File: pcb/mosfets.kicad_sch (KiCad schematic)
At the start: 21 parts, among them IC2 IRFR9014PBF, J15 Arm, J4 Screw_Terminal_01x12, Q1 DMN3404L, Q2 DMN3404L, Q3 DMN3404L, Q4 DMN3404L, Q5 DMN3404L, Q7 MMBT2222A, Q8 DMN3404L

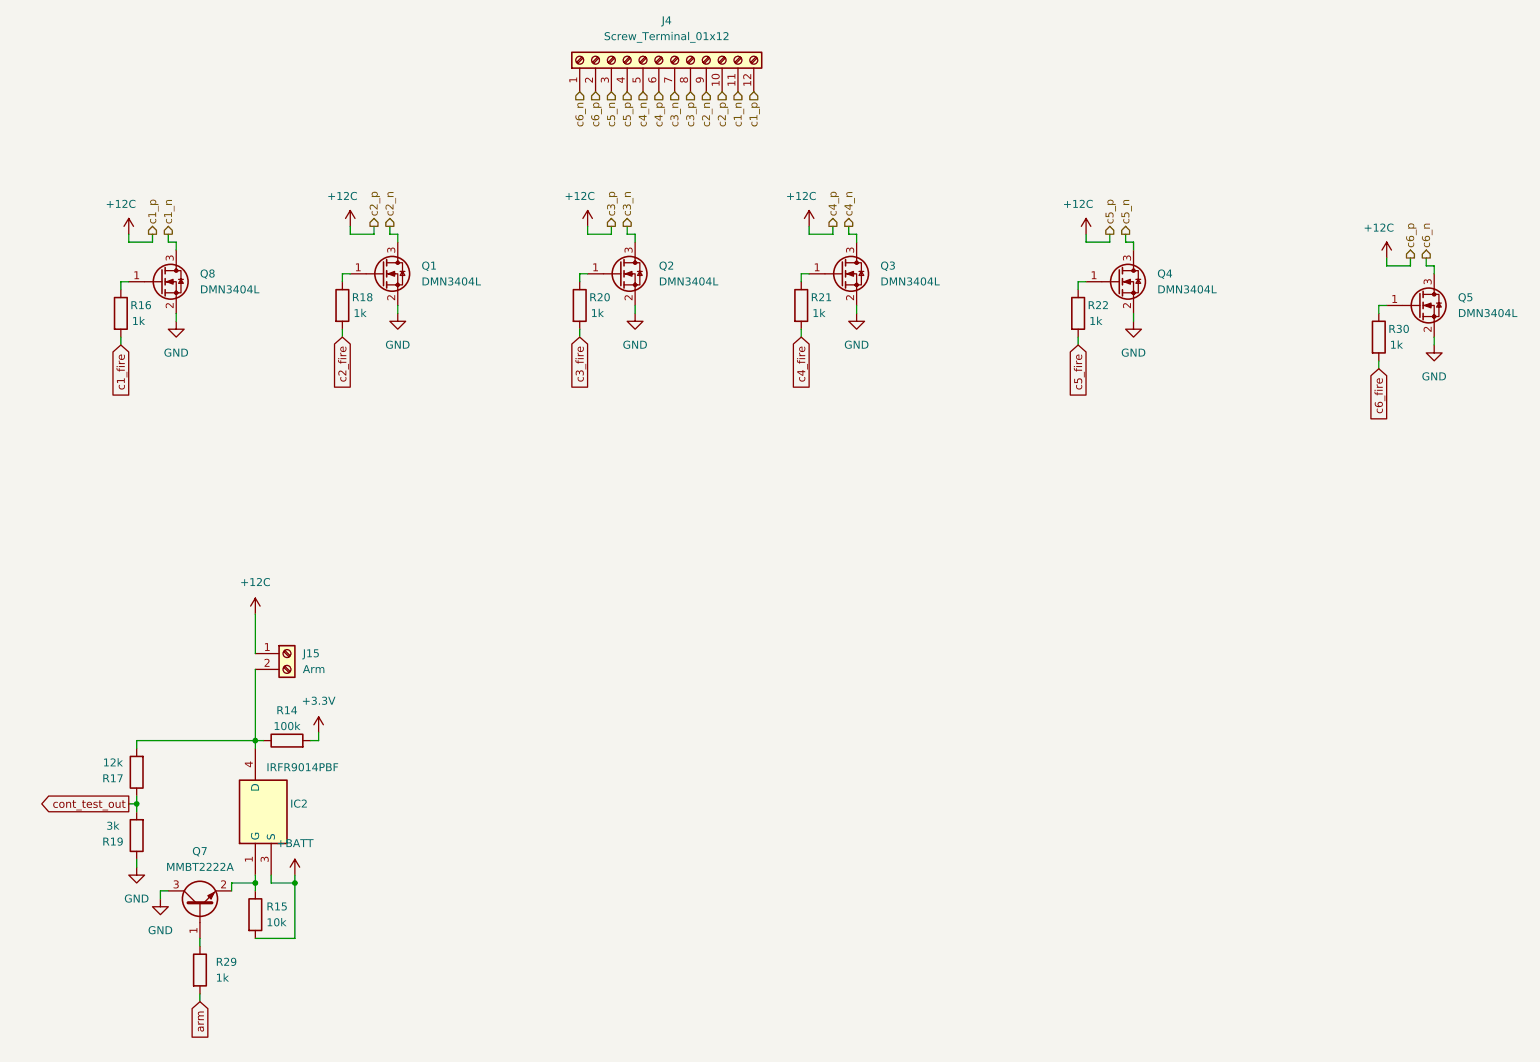
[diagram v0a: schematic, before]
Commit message: added models for some things, fixed micro sd impl and a bunch of other stuff - pcb currently probably ready for production
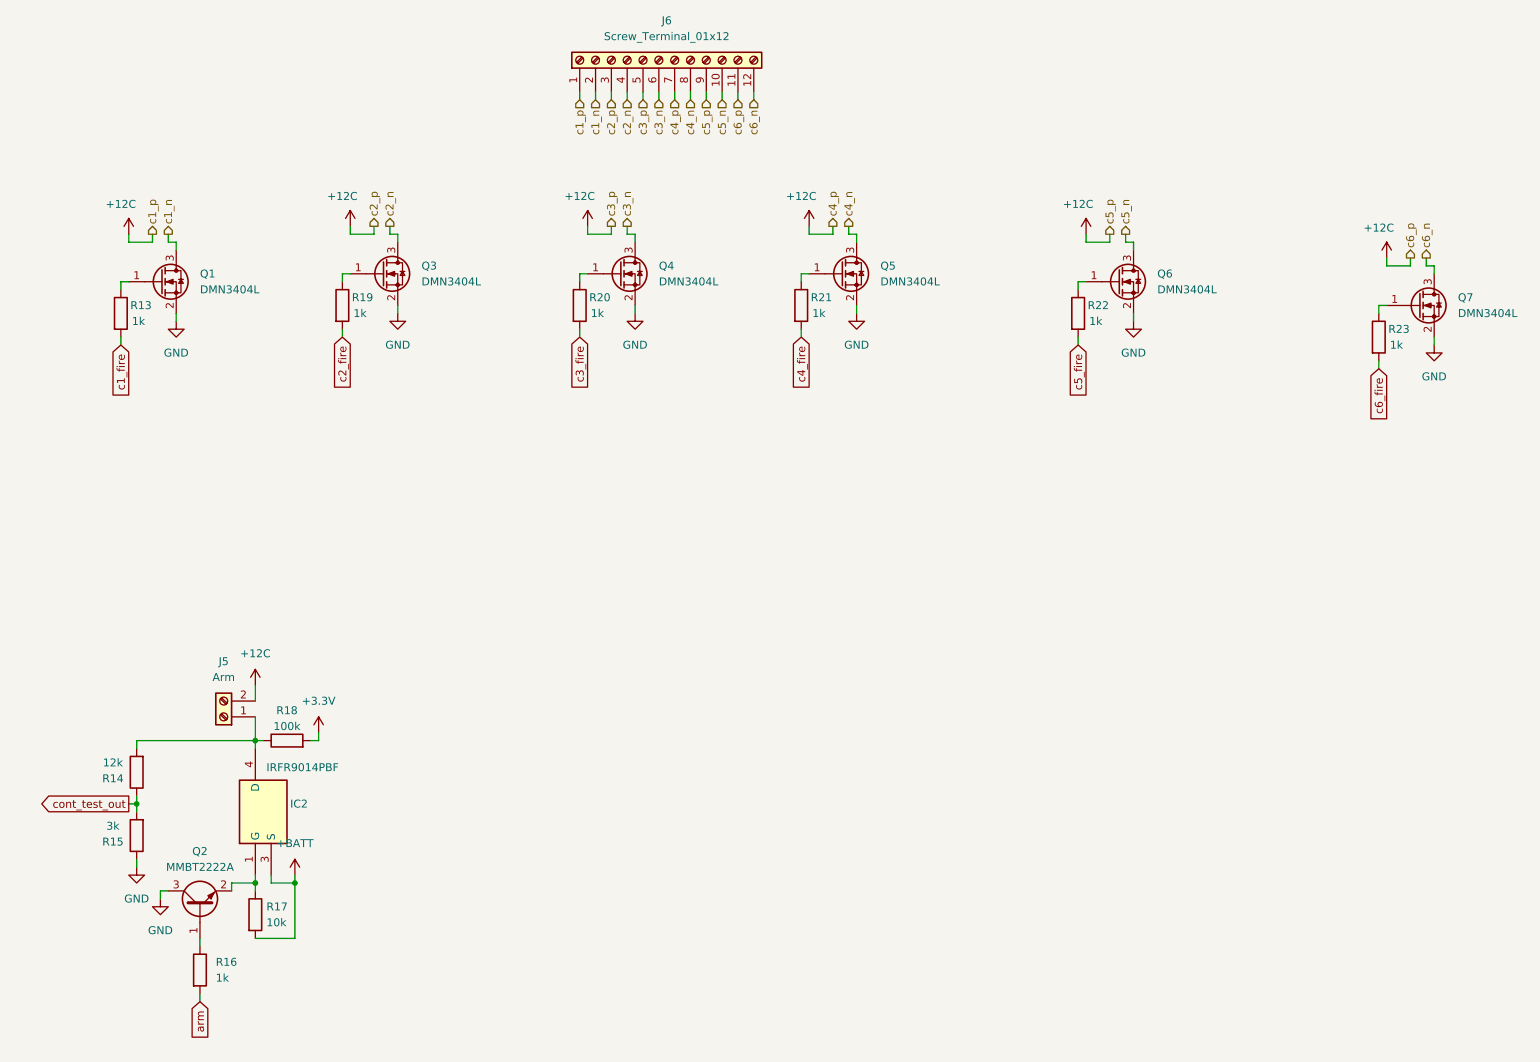
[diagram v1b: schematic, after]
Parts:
- renumbered J15 to J5, J4 to J6, Q8 to Q1, Q7 to Q2, Q1 to Q3, Q2 to Q4, Q3 to Q5, Q4 to Q6, Q5 to Q7, R16 to R13, R17 to R14, R19 to R15, R29 to R16, R15 to R17, R14 to R18, R18 to R19, R30 to R23
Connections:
- net +12C: now also J5.2 (Pin_2), J6.1 (Pin_1), J6.11 (Pin_11), J6.3 (Pin_3), J6.5 (Pin_5), J6.7 (Pin_7), J6.9 (Pin_9); no longer J5.1 (Pin_1), J6.10 (Pin_10), J6.12 (Pin_12), J6.2 (Pin_2), J6.4 (Pin_4), J6.6 (Pin_6), J6.8 (Pin_8)
- net c1_n: now also J6.2 (Pin_2); no longer J6.11 (Pin_11)
- net c2_n: now also J6.4 (Pin_4); no longer J6.9 (Pin_9)
- net c3_n: now also J6.6 (Pin_6); no longer J6.7 (Pin_7)
- net c4_n: now also J6.8 (Pin_8); no longer J6.5 (Pin_5)
- net c5_n: now also J6.10 (Pin_10); no longer J6.3 (Pin_3)
- net c6_n: now also J6.12 (Pin_12); no longer J6.1 (Pin_1)
- net at IC2.4 (D), R14.2, R18.1: now also J5.1 (Pin_1); no longer J5.2 (Pin_2)
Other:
- moved on the sheet: J5

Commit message: updated pcb from schematic changes, also added some length tuning because why not
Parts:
- renumbered J5 to ARM1, J6 to PYRO1
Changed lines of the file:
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@@
 		(dnp no)
 		(fields_autoplaced yes)
-		(property "Reference" "J6"
+		(property "Reference" "PYRO1"
 			(at 125.73 22.86 90)
 			(effects
@@
 			(project ""
 				(path "/d0cafa98-cc2a-4ab3-8dbc-f937bedf434b/95cda17b-9612-4f29-a3fa-5878468b6ce9"
-					(reference "J6")
+					(reference "PYRO1")
 					(unit 1)
 				)
@@
 		(dnp no)
 		(fields_autoplaced yes)
-		(property "Reference" "J5"
+		(property "Reference" "ARM1"
 			(at 54.61 125.73 0)
 			(effects
@@
 			(project ""
 				(path "/d0cafa98-cc2a-4ab3-8dbc-f937bedf434b/95cda17b-9612-4f29-a3fa-5878468b6ce9"
-					(reference "J5")
-					(unit 1)
-				)
+					(reference "ARM1")
+					(unit 1)
+				)

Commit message: mainly worked on bom (still just on google sheets), but while doing so fixed some issues and redid some component selection
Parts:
- removed PYRO1: Screw_Terminal_01x12, TerminalBlock:TerminalBlock_Xinya_XY308-2.54-12P_1x12_P2.54mm_Horizontal, symbol Connector:Screw_Terminal_01x12
- added PYRO1, PYRO2: Screw_Terminal_01x06, footprints:TBC05061GG, symbol Connector:Screw_Terminal_01x06
- ARM1: footprint TerminalBlock:TerminalBlock_Xinya_XY308-2.54-2P_1x02_P2.54mm_Horizontal -> footprints:TBC05021GG
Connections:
- net +12C: now also PYRO1.1 (Pin_1), PYRO1.3 (Pin_3), PYRO1.5 (Pin_5), PYRO2.1 (Pin_1), PYRO2.3 (Pin_3), PYRO2.5 (Pin_5)
- net c1_n: now also PYRO1.2 (Pin_2)
- net c2_n: now also PYRO1.4 (Pin_4)
- net c3_n: now also PYRO1.6 (Pin_6)
- net c4_n: now also PYRO2.2 (Pin_2)
- net c5_n: now also PYRO2.4 (Pin_4)
- net c6_n: now also PYRO2.6 (Pin_6)
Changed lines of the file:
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@@
-	)
-	(symbol
-		(lib_id "Connector:Screw_Terminal_01x12")
-		(at 124.46 29.21 90)
-		(unit 1)
-		(exclude_from_sim no)
-		(in_bom yes)
-		(on_board yes)
-		(dnp no)
-		(fields_autoplaced yes)
-		(property "Reference" "PYRO1"
-			(at 125.73 22.86 90)
-			(effects
-				(font
-					(size 1.27 1.27)
-				)
-			)
-		)
-		(property "Value" "Screw_Terminal_01x12"
-			(at 125.73 25.4 90)
-			(effects
-				(font
-					(size 1.27 1.27)
-				)
-			)
-		)
-		(property "Footprint" "TerminalBlock:TerminalBlock_Xinya_XY308-2.54-12P_1x12_P2.54mm_Horizontal"
-			(at 124.46 29.21 0)
-			(effects
-				(font
-					(size 1.27 1.27)
-				)
-				(hide yes)
-			)
-		)
-		(property "Datasheet" "~"
-			(at 124.46 29.21 0)
-			(effects
-				(font
-					(size 1.27 1.27)
-				)
-				(hide yes)
-			)
-		)
-		(property "Description" "Generic screw terminal, single row, 01x12, script generated (kicad-library-utils/schlib/autogen/connector/)"
-			(at 124.46 29.21 0)
-			(effects
-				(font
-					(size 1.27 1.27)
-				)
-				(hide yes)
-			)
-		)
-		(pin "6"
-		)
-		(pin "10"
-		)
-		(pin "1"
-		)
-		(pin "7"
-		)
-		(pin "5"
-		)
-		(pin "4"
-		)
-		(pin "3"
-		)
-		(pin "12"
-		)
-		(pin "11"
-		)
-		(pin "2"
-		)
-		(pin "9"
-		)
-		(pin "8"
-		)
-		(instances
-			(project ""
-				(path "/d0cafa98-cc2a-4ab3-8dbc-f937bedf434b/95cda17b-9612-4f29-a3fa-5878468b6ce9"
-					(reference "PYRO1")
-					(unit 1)
-				)
-			)
-		)
 	)
 	(symbol
@@
 	)
 	(symbol
+		(lib_id "Connector:Screw_Terminal_01x06")
+		(at 116.84 29.21 90)
+		(unit 1)
+		(exclude_from_sim no)
+		(in_bom yes)
+		(on_board yes)
+		(dnp no)
+		(fields_autoplaced yes)
+		(property "Reference" "PYRO1"
+			(at 118.11 22.86 90)
+			(effects
+				(font
+					(size 1.27 1.27)
+				)
+			)
+		)
+		(property "Value" "Screw_Terminal_01x06"
+			(at 118.11 25.4 90)
+			(effects
+				(font
+					(size 1.27 1.27)
+				)
+			)
+		)
+		(property "Footprint" "footprints:TBC05061GG"
+			(at 116.84 29.21 0)
+			(effects
+				(font
+					(size 1.27 1.27)
+				)
+				(hide yes)
+			)
+		)
+		(property "Datasheet" "~"
+			(at 116.84 29.21 0)
+			(effects
+				(font
+					(size 1.27 1.27)
+				)
+				(hide yes)
+			)
+		)
+		(property "Description" "Generic screw terminal, single row, 01x06, script generated (kicad-library-utils/schlib/autogen/connector/)"
+			(at 116.84 29.21 0)
+			(effects
+				(font
+					(size 1.27 1.27)
+				)
+				(hide yes)
+			)
+		)
+		(pin "2"
+		)
+		(pin "1"
+		)
+		(pin "3"
+		)
+		(pin "6"
+		)
+		(pin "5"
+		)
+		(pin "4"
+		)
+		(instances
+			(project ""
+				(path "/d0cafa98-cc2a-4ab3-8dbc-f937bedf434b/95cda17b-9612-4f29-a3fa-5878468b6ce9"
+					(reference "PYRO1")
+					(unit 1)
+				)
+			)
+		)
+	)
+	(symbol
 		(lib_id "Device:R")
 		(at 38.1 69.85 0)
@@
 			)
 		)
-		(property "Footprint" "TerminalBlock:TerminalBlock_Xinya_XY308-2.54-2P_1x02_P2.54mm_Horizontal"
+		(property "Footprint" "footprints:TBC05021GG"
 			(at 54.61 134.62 0)
 			(effects
@@
 					(unit 1)
 				)
+			)
+		)
+	)
+	(symbol
+		(lib_id "Connector:Screw_Terminal_01x06")
+		(at 132.08 29.21 90)
+		(unit 1)
+		(exclude_from_sim no)
+		(in_bom yes)
+		(on_board yes)
+		(dnp no)
+		(fields_autoplaced yes)
+		(property "Reference" "PYRO2"
+			(at 133.35 22.86 90)
+			(effects
+				(font
+					(size 1.27 1.27)
+				)
+			)
+		)
+		(property "Value" "Screw_Terminal_01x06"
+			(at 133.35 25.4 90)
+			(effects
+				(font
+					(size 1.27 1.27)
+				)
+			)
+		)
+		(property "Footprint" "footprints:TBC05061GG"
+			(at 132.08 29.21 0)
+			(effects
+				(font
+					(size 1.27 1.27)
+				)
+				(hide yes)
+			)
+		)
+		(property "Datasheet" "~"
+			(at 132.08 29.21 0)
+			(effects
+				(font
+					(size 1.27 1.27)
+				)
+				(hide yes)
+			)
+		)
+		(property "Description" "Generic screw terminal, single row, 01x06, script generated (kicad-library-utils/schlib/autogen/connector/)"
+			(at 132.08 29.21 0)
+			(effects
+				(font
+					(size 1.27 1.27)
+				)
+				(hide yes)
+			)
+		)
+		(pin "2"
+		)
+		(pin "1"
+		)
+		(pin "3"
+		)
+		(pin "6"
+		)
+		(pin "5"
+		)
+		(pin "4"
+		)
+		(instances
+			(project "stDevboard"
+				(path "/d0cafa98-cc2a-4ab3-8dbc-f937bedf434b/95cda17b-9612-4f29-a3fa-5878468b6ce9"
+					(reference "PYRO2")
+					(unit 1)
+				)

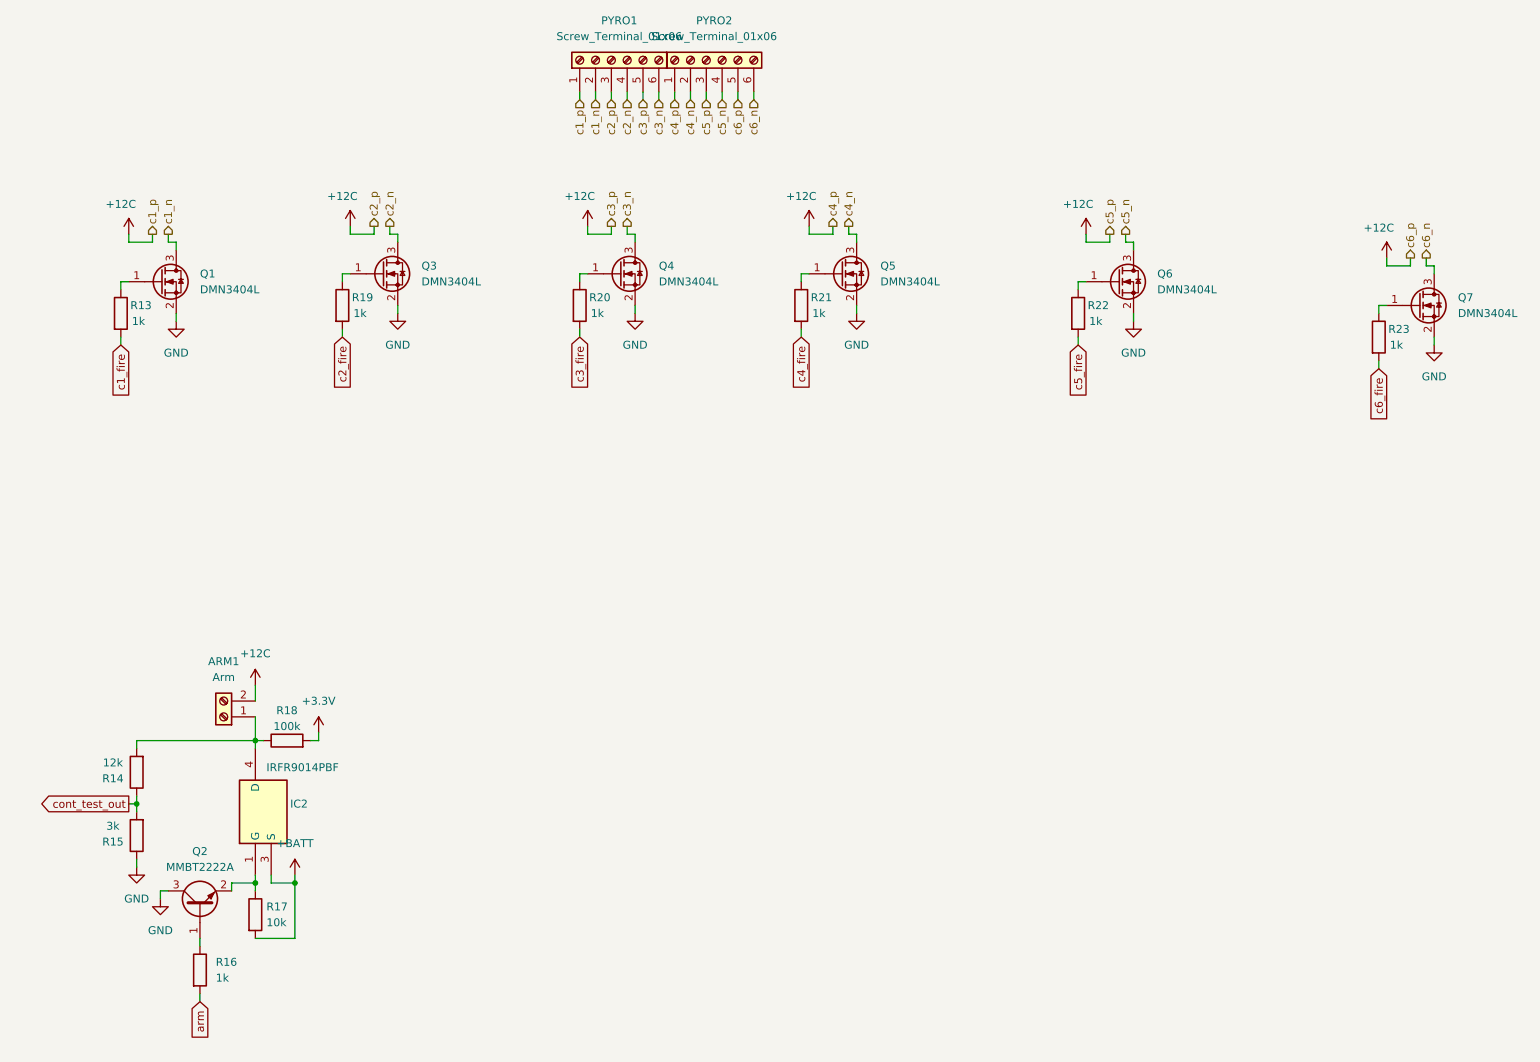
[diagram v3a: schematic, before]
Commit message: reorganized schematic, started to add a readme (not really though), also pcb updated
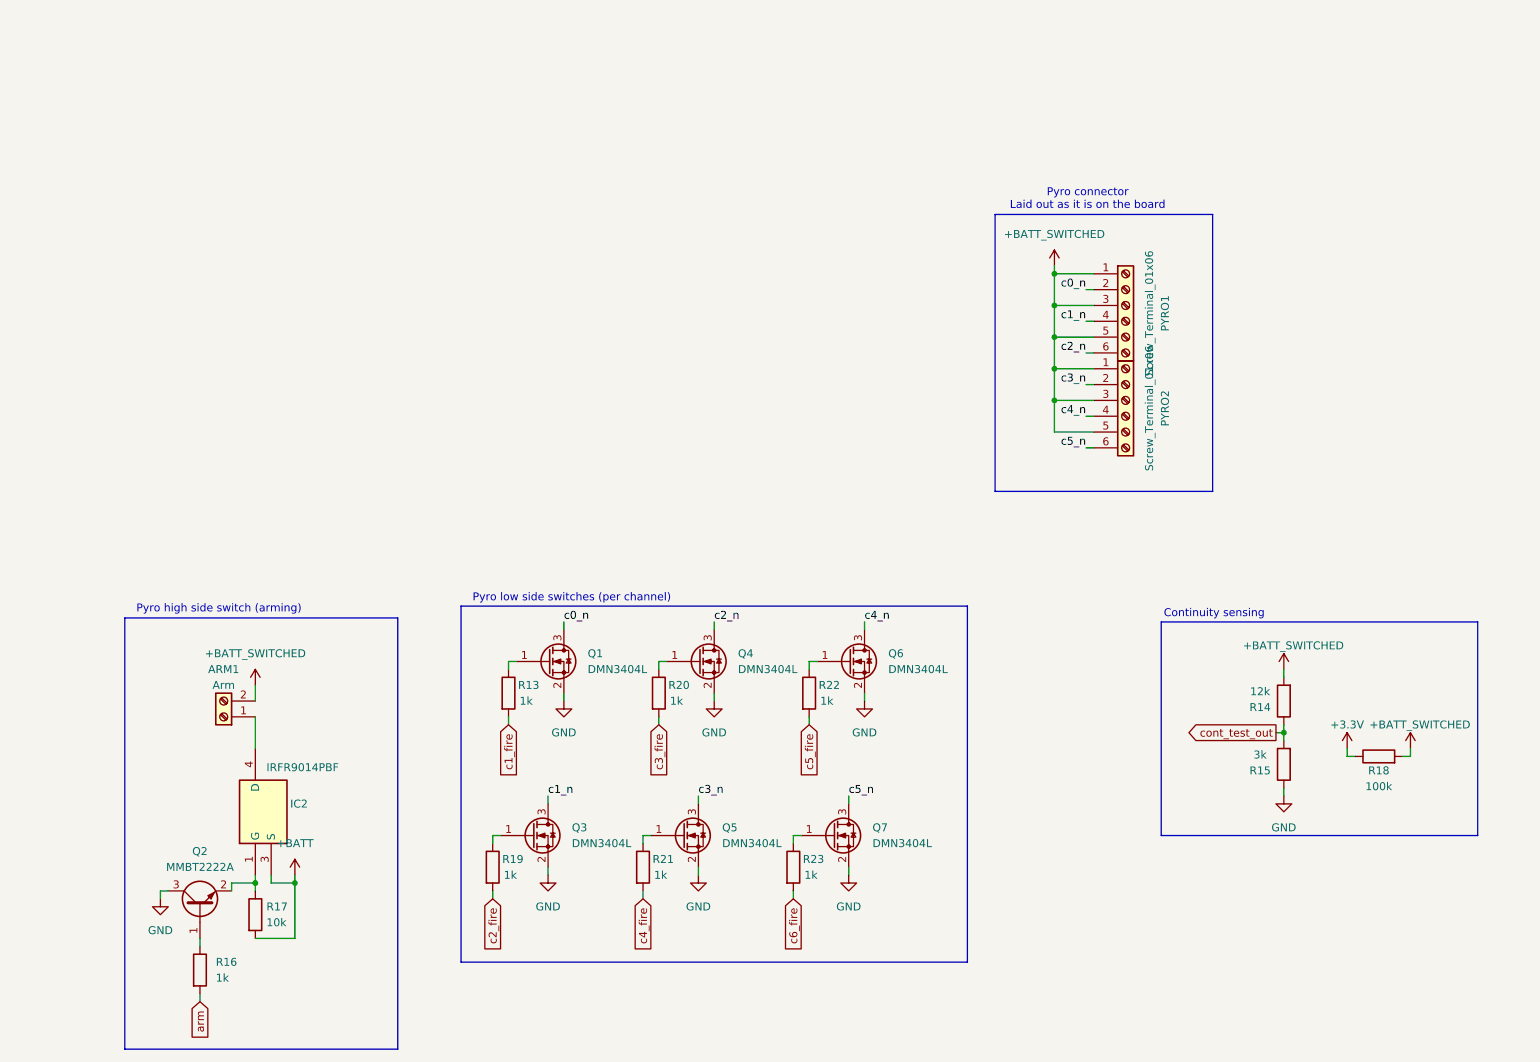
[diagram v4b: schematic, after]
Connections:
- net c6_n is gone; now on net c5_n: PYRO2.6 (Pin_6), Q7.3 (D)
- net +3.3V: now also R18.1; no longer R18.2
- net c1_n: now also PYRO1.4 (Pin_4), Q3.3 (D); no longer PYRO1.2 (Pin_2), Q1.3 (D)
- net c2_n: now also PYRO1.6 (Pin_6), Q4.3 (D); no longer PYRO1.4 (Pin_4), Q3.3 (D)
- net c3_n: now also PYRO2.2 (Pin_2), Q5.3 (D); no longer PYRO1.6 (Pin_6), Q4.3 (D)
- net c4_n: now also PYRO2.4 (Pin_4), Q6.3 (D); no longer PYRO2.2 (Pin_2), Q5.3 (D)
- net c5_n: no longer PYRO2.4 (Pin_4), Q6.3 (D)
- net at ARM1.1 (Pin_1), IC2.4 (D): no longer R14.2, R18.1
- net +12C renamed +BATT_SWITCHED
- net +BATT_SWITCHED: now also R14.2, R18.2
- new net c0_n: PYRO1.2 (Pin_2), Q1.3 (D)
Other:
- note added: "Continuity sensing"
- note added: "Pyro connector Laid out as it is on the board"
- note added: "Pyro high side switch (arming)"
- note added: "Pyro low side switches (per channel)"
- moved on the sheet: PYRO1, PYRO2, Q1, Q3, Q4, Q5, Q6, Q7, R13, R14, R15, R18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
